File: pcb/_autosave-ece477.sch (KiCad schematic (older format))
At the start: 4 parts

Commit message: added sd func
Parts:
- removed 3.3Vto5V: CRE1S0305S3C, Converter_DCDC:Converter_DCDC_muRata_CRE1xxxxxx3C_THT, symbol Regulator_Switching:CRE1S0305S3C
- removed U?: CFAL1602, symbol LED:CFAL1602
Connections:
- wire segments 25 -> 11
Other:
- note removed: "HSPI\nCLK"
- note removed: "HSPI\nMISO"
- note removed: "HSPI\nMOSI"
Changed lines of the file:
@@
 $EndDescr
-$Comp
-L LED:CFAL1602 U?
-U 1 1 5F557C8B
-P 8400 3800
-F 0 "U?" H 8250 3600 50  0001 C CNN
-F 1 "CFAL1602" V 9150 3806 50  0000 R CNN
-F 2 "" H 8250 3600 50  0001 C CNN
-F 3 "" H 8250 3600 50  0001 C CNN
-	1    8400 3800
-	0    -1   -1   0
-$EndComp
-Wire Wire Line
-	7450 2400 7450 2450
 $Comp
 L Connector:Micro_SD_Card J?
@@
 	1    0    0    -1
 $EndComp
-Wire Wire Line
-	5300 3950 7150 3950
-Wire Wire Line
-	7150 3950 7150 3350
-Text Notes 5700 2500 0    50   ~ 0
-HSPI\nMISO
 Wire Bus Line
 	5300 3650 5800 3650
-Connection ~ 5800 3650
 Wire Bus Line
 	5800 3650 5800 5600
 Wire Bus Line
 	5300 3750 6150 3750
-Connection ~ 6150 3750
 Wire Bus Line
 	6150 3750 6150 5600
 Wire Bus Line
 	5300 3850 6500 3850
-Connection ~ 6500 3850
 Wire Bus Line
 	6500 3850 6500 5600
-Text Notes 6050 2500 0    50   ~ 0
-HSPI\nMOSI
-Text Notes 6400 2500 0    50   ~ 0
-HSPI\nCLK
-Wire Wire Line
-	7150 2750 5800 2750
-Wire Wire Line
-	7150 2950 6150 2950
-Wire Wire Line
-	7150 3150 6500 3150
-Wire Bus Line
-	5800 2550 5800 3650
-Wire Bus Line
-	6150 2550 6150 3750
-Wire Bus Line
-	6500 2550 6500 3850
 Wire Wire Line
 	7150 4900 6150 4900
@@
 $EndComp
 Wire Wire Line
-	7650 3650 7650 3950
-Wire Wire Line
-	7650 3950 8800 3950
-Wire Wire Line
 	7150 5000 6950 5000
-Wire Wire Line
-	6950 5000 6950 4150
-Wire Wire Line
-	9250 4150 9250 1450
-Wire Wire Line
-	6950 4150 9250 4150
 Wire Bus Line
 	10150 1450 2800 1450
@@
 Wire Wire Line
 	4300 2450 4300 1450
-$Comp
-L Regulator_Switching:CRE1S0305S3C 3.3Vto5V
-U 1 1 5F59D7B7
-P 8150 2000
-F 0 "3.3Vto5V" H 8150 2467 50  0000 C CNN
-F 1 "CRE1S0305S3C" H 8150 2376 50  0000 C CNN
-F 2 "Converter_DCDC:Converter_DCDC_muRata_CRE1xxxxxx3C_THT" H 8150 1600 50  0001 C CNN
-F 3 "http://power.murata.com/datasheet?/data/power/ncl/kdc_cre1.pdf" H 8150 1500 50  0001 C CNN
-	1    8150 2000
-	1    0    0    -1
-$EndComp
-Wire Wire Line
-	7650 1800 7650 1450
-Wire Wire Line
-	8650 1800 8800 1800
-Wire Wire Line
-	8800 1800 8800 3950
-$Comp
-L power:GND #PWR?
-U 1 1 5F5A1A31
-P 7650 2200
-F 0 "#PWR?" H 7650 1950 50  0001 C CNN
-F 1 "GND" H 7655 2027 50  0000 C CNN
-F 2 "" H 7650 2200 50  0001 C CNN
-F 3 "" H 7650 2200 50  0001 C CNN
-	1    7650 2200
-	1    0    0    -1
-$EndComp
-$Comp
-L power:GND #PWR?
-U 1 1 5F5A1F8A
-P 8650 2200
-F 0 "#PWR?" H 8650 1950 50  0001 C CNN
-F 1 "GND" H 8655 2027 50  0000 C CNN
-F 2 "" H 8650 2200 50  0001 C CNN
-F 3 "" H 8650 2200 50  0001 C CNN
-	1    8650 2200
-	1    0    0    -1
-$EndComp
-$Comp
-L power:GND #PWR?
-U 1 1 5F5A2D81
-P 7450 3650
-F 0 "#PWR?" H 7450 3400 50  0001 C CNN
-F 1 "GND" H 7455 3477 50  0000 C CNN
-F 2 "" H 7450 3650 50  0001 C CNN
-F 3 "" H 7450 3650 50  0001 C CNN
-	1    7450 3650
-	1    0    0    -1
-$EndComp
 Wire Wire Line
 	7000 5200 7150 5200

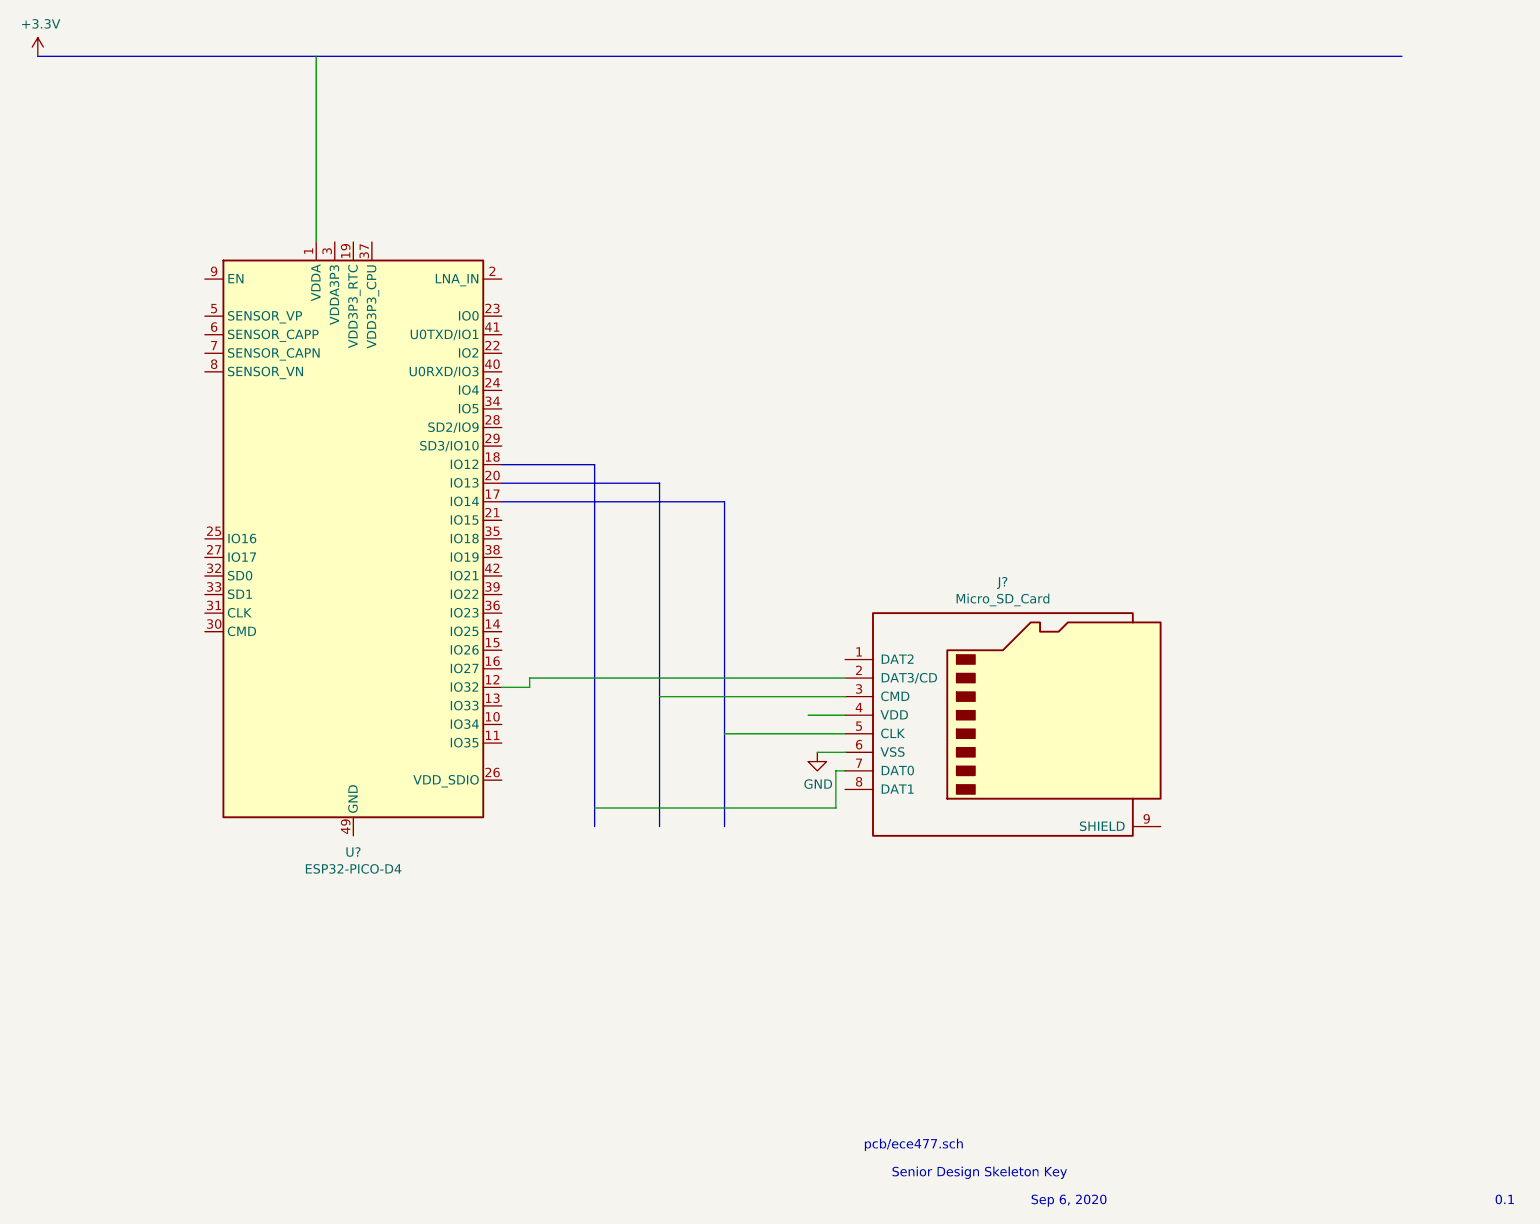
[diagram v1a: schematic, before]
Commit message: connected fingerprint scanner in schematic
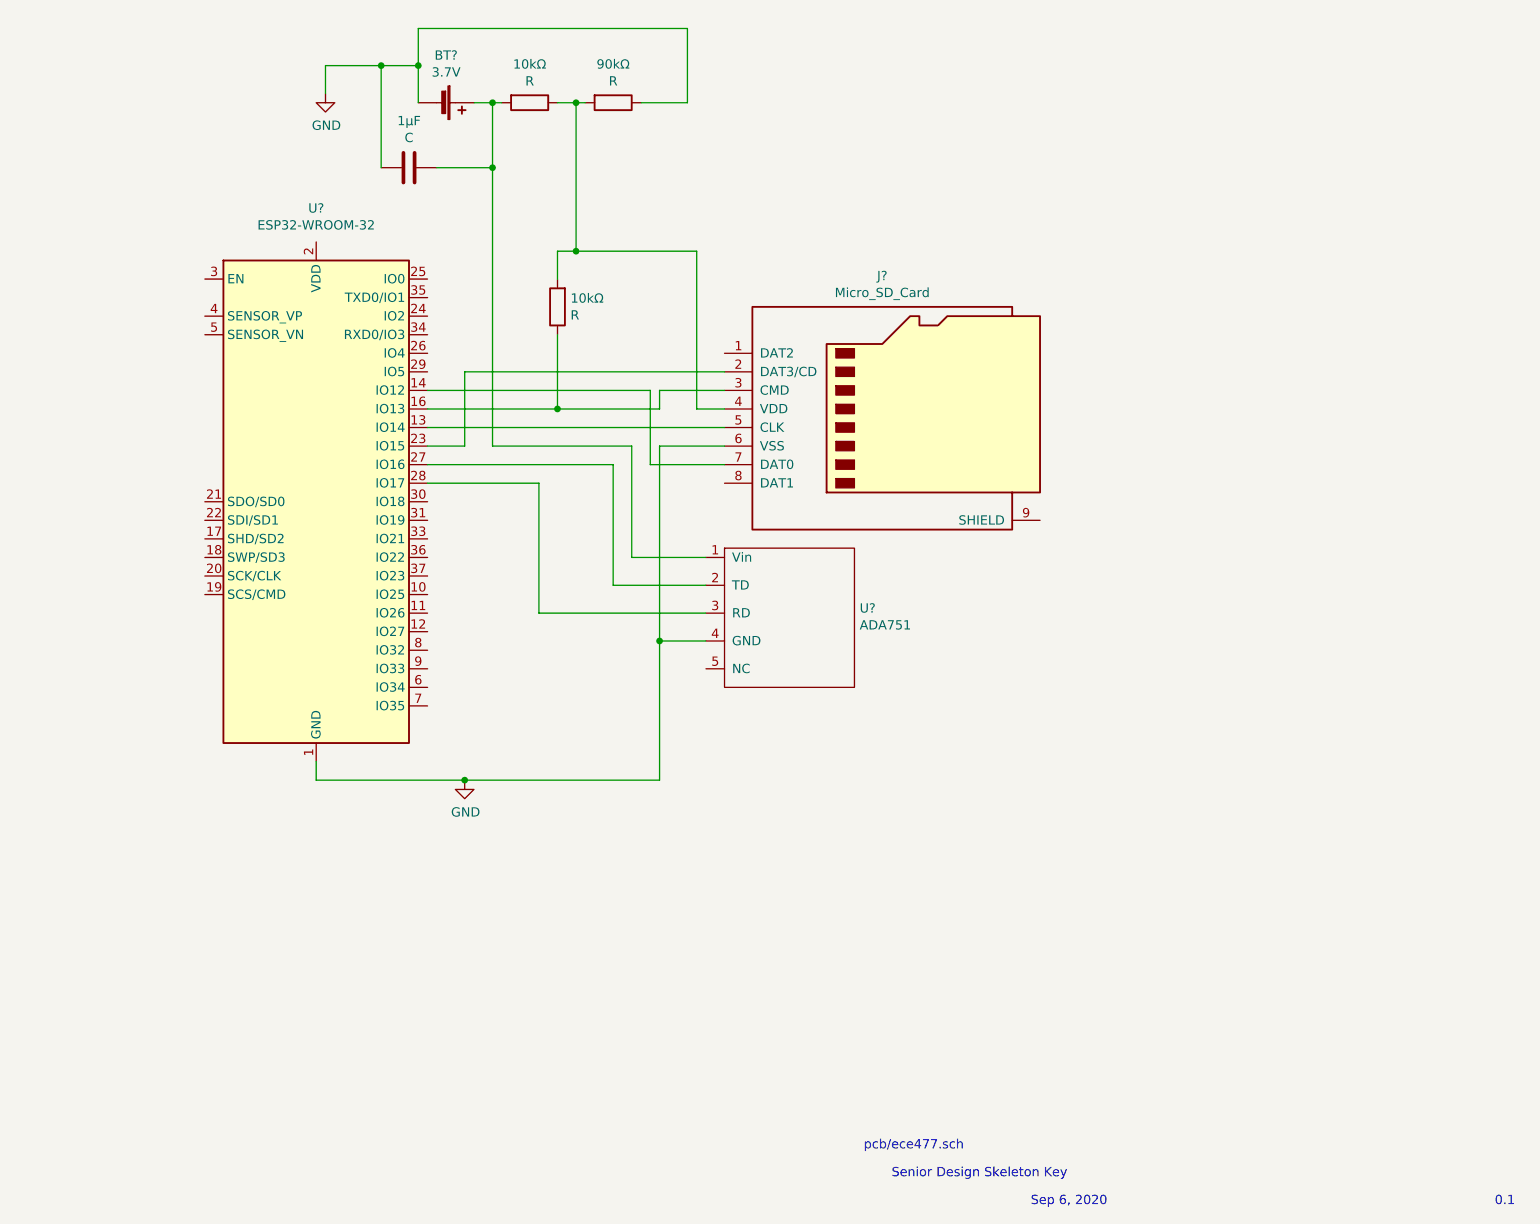
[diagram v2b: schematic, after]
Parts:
- removed U?: ESP32-PICO-D4, Package_DFN_QFN:QFN-48-1EP_7x7mm_P0.5mm_EP5.3x5.3mm, symbol RF_Module:ESP32-PICO-D4
- added 10kΩ (x2), 90kΩ: R, symbol Device:R
- added 1µF: C, symbol Device:C
- added BT?: 3.7V, symbol Device:Battery_Cell
- added U?: ADA751, symbol Device:ADA751
- added U?: ESP32-WROOM-32, RF_Module:ESP32-WROOM-32, symbol RF_Module:ESP32-WROOM-32
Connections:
- net labels removed: +3.3V
- wire segments 11 -> 50
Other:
- moved on the sheet: J?
